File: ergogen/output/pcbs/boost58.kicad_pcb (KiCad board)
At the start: 2 copper layers, 144.3 x 128.5 mm, 104 parts, among them SW1 %R, SW10 %R, SW11 %R, SW12 %R, SW13 %R, SW14 %R, SW15 %R, SW16 %R, SW17 %R, SW18 %R, SW19 %R, SW2 %R, SW20 %R, SW21 %R, SW22 %R, SW23 %R, SW24 %R, SW25 %R, SW26 %R, SW27 %R, SW28 %R, SW29 %R, SW3 %R, SW4 %R, SW5 %R, SW6 %R, SW7 %R, SW8 %R, SW9 %R

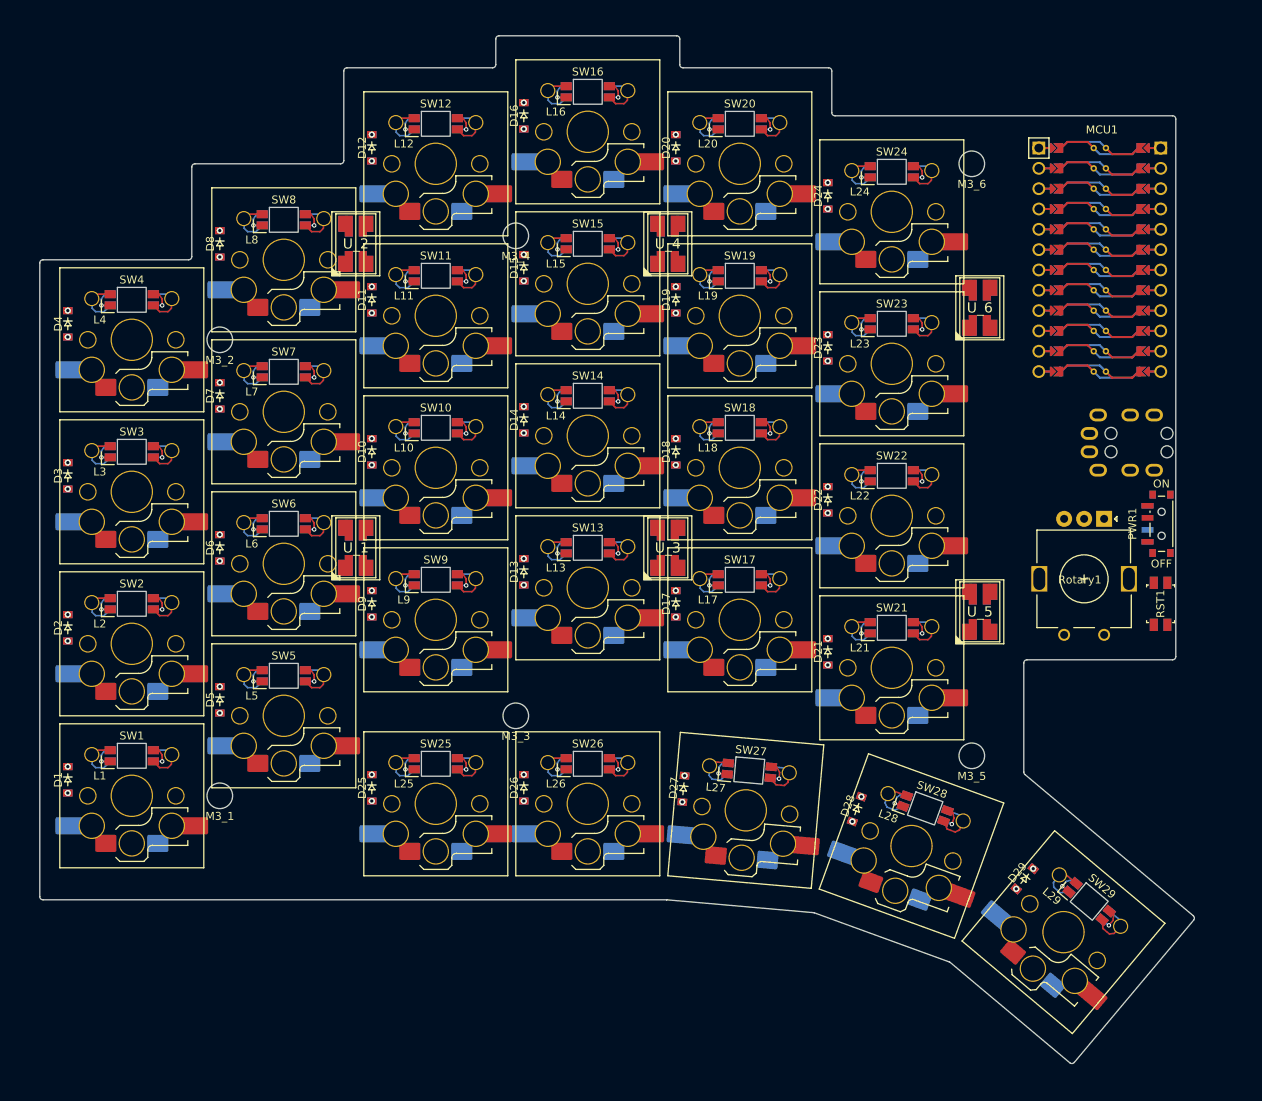
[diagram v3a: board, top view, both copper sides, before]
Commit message: re-generated pcb and ran FreeRouting
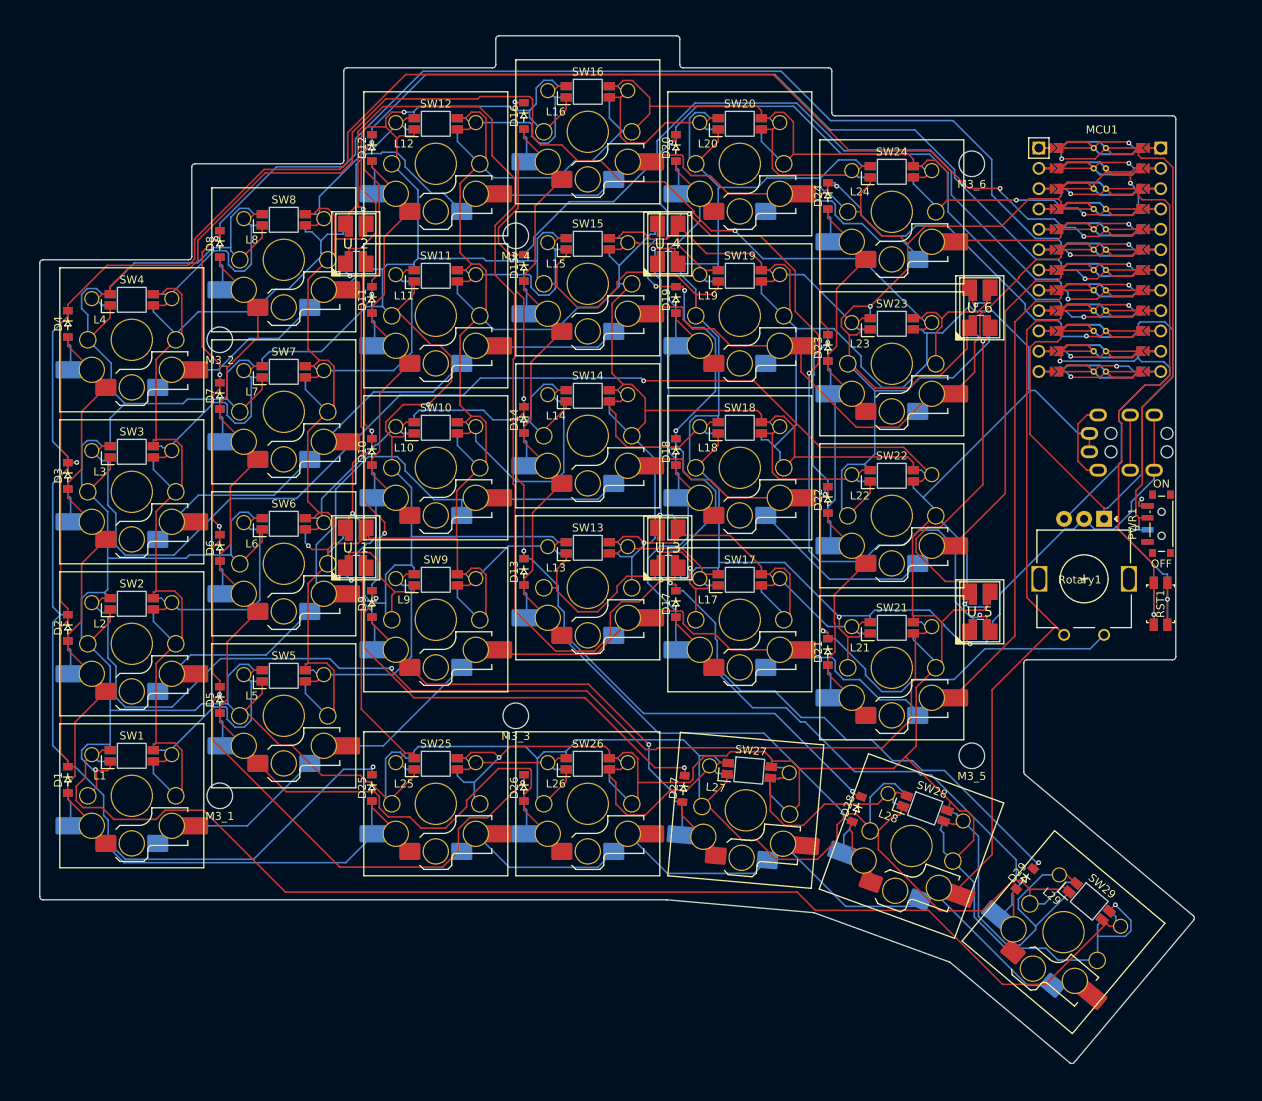
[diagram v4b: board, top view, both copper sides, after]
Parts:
- D1, D10, D11, D12, D13, D14, D15, D16, D17, D18, D19, D2, D20, D21, D22, D23, D24, D25, D26, D27, D28, D29, D3, D4, D5, D6, D7, D8, D9, L1, L10, L11, L12, L13, L14, L15, L16, L17, L18, L19, L2, L20, L21, L22, L23, L24, L25, L26, L27, L28, L29, L3, L4, L5, L6, L7, L8, L9, SW1, SW10, SW11, SW12, SW13, SW14, SW15, SW16, SW17, SW18, SW19, SW2, SW20, SW21, SW22, SW23, SW24, SW25, SW26, SW27, SW28, SW29, SW3, SW4, SW5, SW6, SW7, SW8, SW9: value %R -> ${REFERENCE}
- U_1, U_2, U_3, U_4, U_5, U_6: value (none) -> ${REFERENCE}
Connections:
- SW1 pad : LED11 -> GND
- SW10 pad : LED23 -> GND
- SW11 pad : LED33 -> GND
- SW12 pad : LED43 -> GND
- SW13 pad : LED14 -> GND
- SW14 pad : LED24 -> GND
- SW15 pad : LED34 -> GND
- SW16 pad : LED44 -> GND
- SW17 pad : LED15 -> GND
- SW18 pad : LED25 -> GND
- SW19 pad : LED35 -> GND
- SW2 pad : LED21 -> GND
- SW20 pad : LED45 -> GND
- SW21 pad : LED20 -> GND
- SW22 pad : LED30 -> GND
- SW23 pad : LED40 -> GND
- SW24 pad : LED -> GND
- SW25 pad : LED02 -> GND
- SW26 pad : LED03 -> GND
- SW27 pad : LED04 -> GND
- SW28 pad : LED05 -> GND
- SW29 pad : LED10 -> GND
- SW3 pad : LED31 -> GND
- SW4 pad : LED41 -> GND
- SW5 pad : LED12 -> GND
- SW6 pad : LED22 -> GND
- SW7 pad : LED32 -> GND
- SW8 pad : LED42 -> GND
- SW9 pad : LED13 -> GND
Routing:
- net GND: track 96.3 -> 1173.3 mm, vias 29 -> 9
- net VCC: track 96.3 -> 1073.1 mm, vias 29 -> 6
- net P21: track 0.00 -> 335.4 mm, vias 5 -> 4
- net P20: track 0.00 -> 263.0 mm, vias 5 -> 6
- net P19: track 0.00 -> 233.6 mm, vias 5 -> 7
- net P18: track 0.00 -> 225.9 mm, vias 5 -> 6
- net P15: track 0.00 -> 219.6 mm, vias 5 -> 7
- net P5: track 0.00 -> 203.1 mm, vias 0 -> 1
- net P6: track 0.00 -> 202.8 mm, vias 0 -> 1
- net P4: track 0.00 -> 202.1 mm, vias 0 -> 1
- net DP15: track 0.00 -> 183.4 mm, vias 5 -> 0
- net P2: track 0.00 -> 173.7 mm, vias 0 -> 1
- net P3: track 0.00 -> 172.7 mm, vias 0 -> 1
- net DP18: track 0.00 -> 169.8 mm, vias 5 -> 0
- net DP20: track 0.00 -> 166.1 mm, vias 5 -> 0
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
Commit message: flipped routes for underglow to make routing shorter and hopefully easier
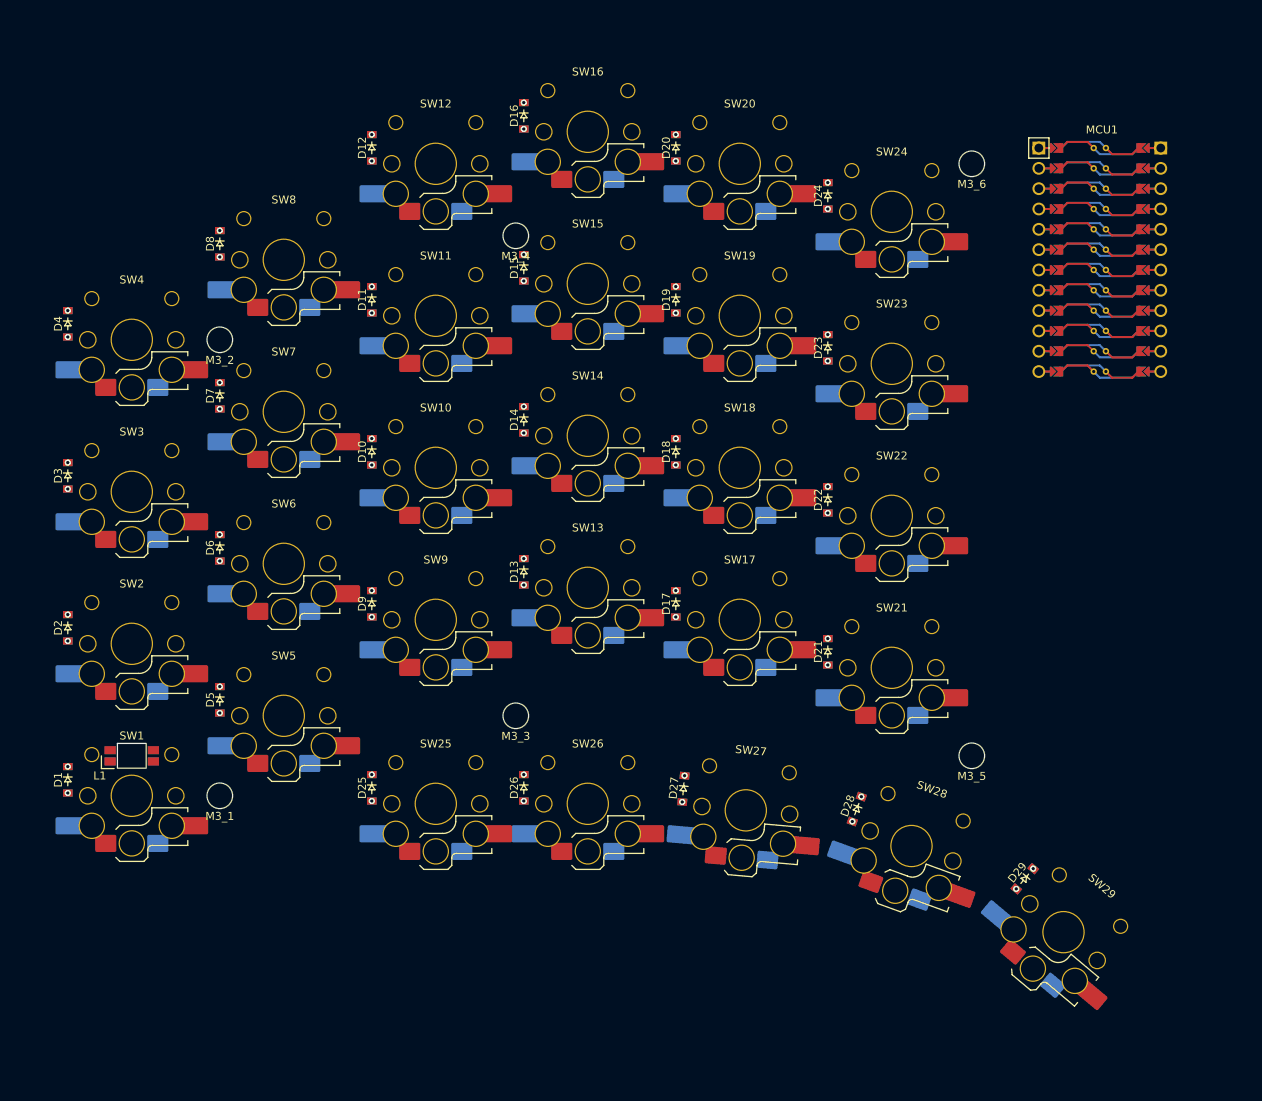
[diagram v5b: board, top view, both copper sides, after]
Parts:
- removed L10, L11, L12, L13, L14, L15, L16, L17, L18, L19, L2, L20, L21, L22, L23, L24, L25, L26, L27, L28, L29, L3, L4, L5, L6, L7, L8, L9: ${REFERENCE}, ceoloide:led_SK6812mini-e (per-key, reversible)
- removed PWR1: , ceoloide:power_switch_smd_side
- removed RST1: , ceoloide:reset_switch_smd_side
- removed Rotary1: , rotary_encoder
- removed TRRS1: TRRS-PJ-320A-dual, TRRS-PJ-320A-dual
- removed U_1, U_2, U_3, U_4, U_5, U_6: ${REFERENCE}, WS2812B
- D1, D10, D11, D12, D13, D14, D15, D16, D17, D18, D19, D2, D20, D21, D22, D23, D24, D25, D26, D27, D28, D29, D3, D4, D5, D6, D7, D8, D9, L1, SW1, SW10, SW11, SW12, SW13, SW14, SW15, SW16, SW17, SW18, SW19, SW2, SW20, SW21, SW22, SW23, SW24, SW25, SW26, SW27, SW28, SW29, SW3, SW4, SW5, SW6, SW7, SW8, SW9: value ${REFERENCE} -> %R
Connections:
- SW1 pad : GND -> LED11
- SW10 pad : GND -> LED23
- SW11 pad : GND -> LED33
- SW12 pad : GND -> LED43
- SW13 pad : GND -> LED14
- SW14 pad : GND -> LED24
- SW15 pad : GND -> LED34
- SW16 pad : GND -> LED44
- SW17 pad : GND -> LED15
- SW18 pad : GND -> LED25
- SW19 pad : GND -> LED35
- SW2 pad : GND -> LED21
- SW20 pad : GND -> LED45
- SW21 pad : GND -> LED20
- SW22 pad : GND -> LED30
- SW23 pad : GND -> LED40
- SW24 pad : GND -> LED
- SW25 pad : GND -> LED02
- SW26 pad : GND -> LED03
- SW27 pad : GND -> LED04
- SW28 pad : GND -> LED05
- SW29 pad : GND -> LED10
- SW3 pad : GND -> LED31
- SW4 pad : GND -> LED41
- SW5 pad : GND -> LED12
- SW6 pad : GND -> LED22
- SW7 pad : GND -> LED32
- SW8 pad : GND -> LED42
- SW9 pad : GND -> LED13
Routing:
- net GND: track 1173.3 -> 0.00 mm, vias 9 -> 0
- net VCC: track 1073.1 -> 0.00 mm, vias 6 -> 0
- net P21: track 335.4 -> 0.00 mm, vias 4 -> 5
- net P20: track 263.0 -> 0.00 mm, vias 6 -> 5
- net P19: track 233.6 -> 0.00 mm, vias 7 -> 5
- net P18: track 225.9 -> 0.00 mm, vias 6 -> 5
- net P15: track 219.6 -> 0.00 mm, vias 7 -> 5
- net P5: track 203.1 -> 0.00 mm, vias 1 -> 0
- net P6: track 202.8 -> 0.00 mm, vias 1 -> 0
- net P4: track 202.1 -> 0.00 mm, vias 1 -> 0
- net DP15: track 183.4 -> 0.00 mm, vias 0 -> 5
- net P2: track 173.7 -> 0.00 mm, vias 1 -> 0
- net P3: track 172.7 -> 0.00 mm, vias 1 -> 0
- net DP18: track 169.8 -> 0.00 mm, vias 0 -> 5
- net DP20: track 166.1 -> 0.00 mm, vias 0 -> 5
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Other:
- board size 144.3 x 128.5 mm -> 3.6 x 3.1 mm

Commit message: re-generated PCB and applied FreeRouting
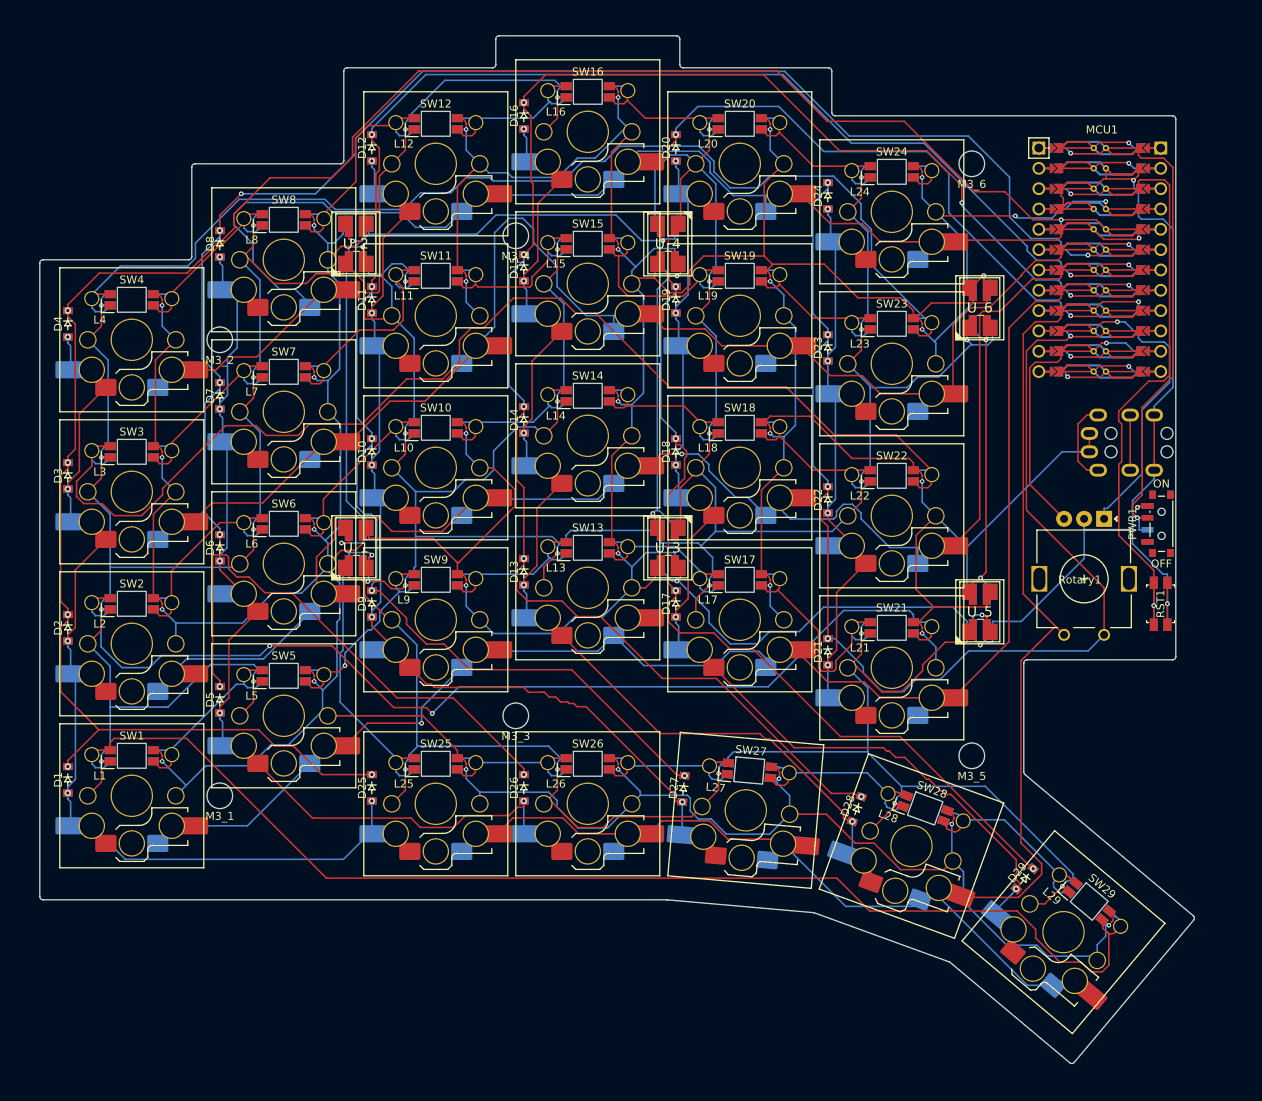
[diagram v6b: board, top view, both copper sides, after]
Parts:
- added L10: ${REFERENCE}, ceoloide:led_SK6812mini-e (per-key, reversible), B.Cu at (78.0, 74.0)
- added L11: ${REFERENCE}, ceoloide:led_SK6812mini-e (per-key, reversible), B.Cu at (78.0, 55.0)
- added L12: ${REFERENCE}, ceoloide:led_SK6812mini-e (per-key, reversible), B.Cu at (78.0, 36.0)
- added L13: ${REFERENCE}, ceoloide:led_SK6812mini-e (per-key, reversible), B.Cu at (97.0, 89.0)
- added L14: ${REFERENCE}, ceoloide:led_SK6812mini-e (per-key, reversible), B.Cu at (97.0, 70.0)
- added L15: ${REFERENCE}, ceoloide:led_SK6812mini-e (per-key, reversible), B.Cu at (97.0, 51.0)
- added L16: ${REFERENCE}, ceoloide:led_SK6812mini-e (per-key, reversible), B.Cu at (97.0, 32.0)
- added L17: ${REFERENCE}, ceoloide:led_SK6812mini-e (per-key, reversible), B.Cu at (116.0, 93.0)
- added L18: ${REFERENCE}, ceoloide:led_SK6812mini-e (per-key, reversible), B.Cu at (116.0, 74.0)
- added L19: ${REFERENCE}, ceoloide:led_SK6812mini-e (per-key, reversible), B.Cu at (116.0, 55.0)
- added L2: ${REFERENCE}, ceoloide:led_SK6812mini-e (per-key, reversible), B.Cu at (40.0, 96.0)
- added L20: ${REFERENCE}, ceoloide:led_SK6812mini-e (per-key, reversible), B.Cu at (116.0, 36.0)
- added L21: ${REFERENCE}, ceoloide:led_SK6812mini-e (per-key, reversible), B.Cu at (135.0, 99.0)
- added L22: ${REFERENCE}, ceoloide:led_SK6812mini-e (per-key, reversible), B.Cu at (135.0, 80.0)
- added L23: ${REFERENCE}, ceoloide:led_SK6812mini-e (per-key, reversible), B.Cu at (135.0, 61.0)
- added L24: ${REFERENCE}, ceoloide:led_SK6812mini-e (per-key, reversible), B.Cu at (135.0, 42.0)
- added L25: ${REFERENCE}, ceoloide:led_SK6812mini-e (per-key, reversible), B.Cu at (78.0, 116.0)
- added L26: ${REFERENCE}, ceoloide:led_SK6812mini-e (per-key, reversible), B.Cu at (97.0, 116.0)
- added L27: ${REFERENCE}, ceoloide:led_SK6812mini-e (per-key, reversible), B.Cu at (117.2, 116.8)
- added L28: ${REFERENCE}, ceoloide:led_SK6812mini-e (per-key, reversible), B.Cu at (139.2, 121.6)
- added L29: ${REFERENCE}, ceoloide:led_SK6812mini-e (per-key, reversible), B.Cu at (159.7, 133.2)
- added L3: ${REFERENCE}, ceoloide:led_SK6812mini-e (per-key, reversible), B.Cu at (40.0, 77.0)
- added L4: ${REFERENCE}, ceoloide:led_SK6812mini-e (per-key, reversible), B.Cu at (40.0, 58.0)
- added L5: ${REFERENCE}, ceoloide:led_SK6812mini-e (per-key, reversible), B.Cu at (59.0, 105.0)
- added L6: ${REFERENCE}, ceoloide:led_SK6812mini-e (per-key, reversible), B.Cu at (59.0, 86.0)
- added L7: ${REFERENCE}, ceoloide:led_SK6812mini-e (per-key, reversible), B.Cu at (59.0, 67.0)
- added L8: ${REFERENCE}, ceoloide:led_SK6812mini-e (per-key, reversible), B.Cu at (59.0, 48.0)
- added L9: ${REFERENCE}, ceoloide:led_SK6812mini-e (per-key, reversible), B.Cu at (78.0, 93.0)
- added PWR1: , ceoloide:power_switch_smd_side, F.Cu at (168.7, 86.0)
- added RST1: , ceoloide:reset_switch_smd_side, F.Cu at (168.6, 96.0)
- added Rotary1: , rotary_encoder, F.Cu at (159.0, 93.0)
- added TRRS1: TRRS-PJ-320A-dual, TRRS-PJ-320A-dual, F.Cu at (171.0, 77.0)
- added U_1: ${REFERENCE}, WS2812B, F.Cu at (68.0, 89.0)
- added U_2: ${REFERENCE}, WS2812B, F.Cu at (68.0, 51.0)
- added U_3: ${REFERENCE}, WS2812B, F.Cu at (107.0, 89.0)
- added U_4: ${REFERENCE}, WS2812B, F.Cu at (107.0, 51.0)
- added U_5: ${REFERENCE}, WS2812B, F.Cu at (146.0, 97.0)
- added U_6: ${REFERENCE}, WS2812B, F.Cu at (146.0, 59.0)
- D1, D10, D11, D12, D13, D14, D15, D16, D17, D18, D19, D2, D20, D21, D22, D23, D24, D25, D26, D27, D28, D29, D3, D4, D5, D6, D7, D8, D9, L1, SW1, SW10, SW11, SW12, SW13, SW14, SW15, SW16, SW17, SW18, SW19, SW2, SW20, SW21, SW22, SW23, SW24, SW25, SW26, SW27, SW28, SW29, SW3, SW4, SW5, SW6, SW7, SW8, SW9: value %R -> ${REFERENCE}
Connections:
- SW1 pad : LED11 -> GND
- SW10 pad : LED23 -> GND
- SW11 pad : LED33 -> GND
- SW12 pad : LED43 -> GND
- SW13 pad : LED14 -> GND
- SW14 pad : LED24 -> GND
- SW15 pad : LED34 -> GND
- SW16 pad : LED44 -> GND
- SW17 pad : LED15 -> GND
- SW18 pad : LED25 -> GND
- SW19 pad : LED35 -> GND
- SW2 pad : LED21 -> GND
- SW20 pad : LED45 -> GND
- SW21 pad : LED20 -> GND
- SW22 pad : LED30 -> GND
- SW23 pad : LED40 -> GND
- SW24 pad : LED -> GND
- SW25 pad : LED02 -> GND
- SW26 pad : LED03 -> GND
- SW27 pad : LED04 -> GND
- SW28 pad : LED05 -> GND
- SW29 pad : LED10 -> GND
- SW3 pad : LED31 -> GND
- SW4 pad : LED41 -> GND
- SW5 pad : LED12 -> GND
- SW6 pad : LED22 -> GND
- SW7 pad : LED32 -> GND
- SW8 pad : LED42 -> GND
- SW9 pad : LED13 -> GND
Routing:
- net GND: track 0.00 -> 957.5 mm, vias 0 -> 34
- net VCC: track 0.00 -> 894.7 mm, vias 0 -> 31
- net P21: track 0.00 -> 257.6 mm, vias 5 -> 6
- net P20: track 0.00 -> 250.8 mm, vias 5 -> 7
- net P19: track 0.00 -> 221.9 mm, vias 5 -> 6
- net P18: track 0.00 -> 210.7 mm, vias 5 -> 7
- net P6: track 0.00 -> 208.1 mm, vias 0 -> 1
- net P5: track 0.00 -> 201.4 mm, vias 0 -> 2
- net P15: track 0.00 -> 198.4 mm, vias 5 -> 6
- net P4: track 0.00 -> 198.3 mm, vias 0 -> 2
- net P3: track 0.00 -> 188.5 mm, vias 0 -> 1
- net P2: track 0.00 -> 186.2 mm, vias 0 -> 1
- net LED10: track 0.00 -> 159.4 mm
- net P14: track 0.00 -> 157.5 mm, vias 4 -> 5
- net LED30: track 0.00 -> 152.4 mm
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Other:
- board size 3.6 x 3.1 mm -> 144.3 x 128.5 mm
